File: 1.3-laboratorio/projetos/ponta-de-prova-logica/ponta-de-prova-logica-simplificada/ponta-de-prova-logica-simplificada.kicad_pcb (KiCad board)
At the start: 2 copper layers, 66 x 45.7 mm, 25 parts, among them J1 Conn_01x02, J2 TP1, SW1 SW_DPDT_x2, U1 LM339

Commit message: Ajustes finos no leiaute da PCB.
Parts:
- moved PP1 1.52 mm to (63.5, 46.7)
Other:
- board text added: "Ponta de Prova Lógica"

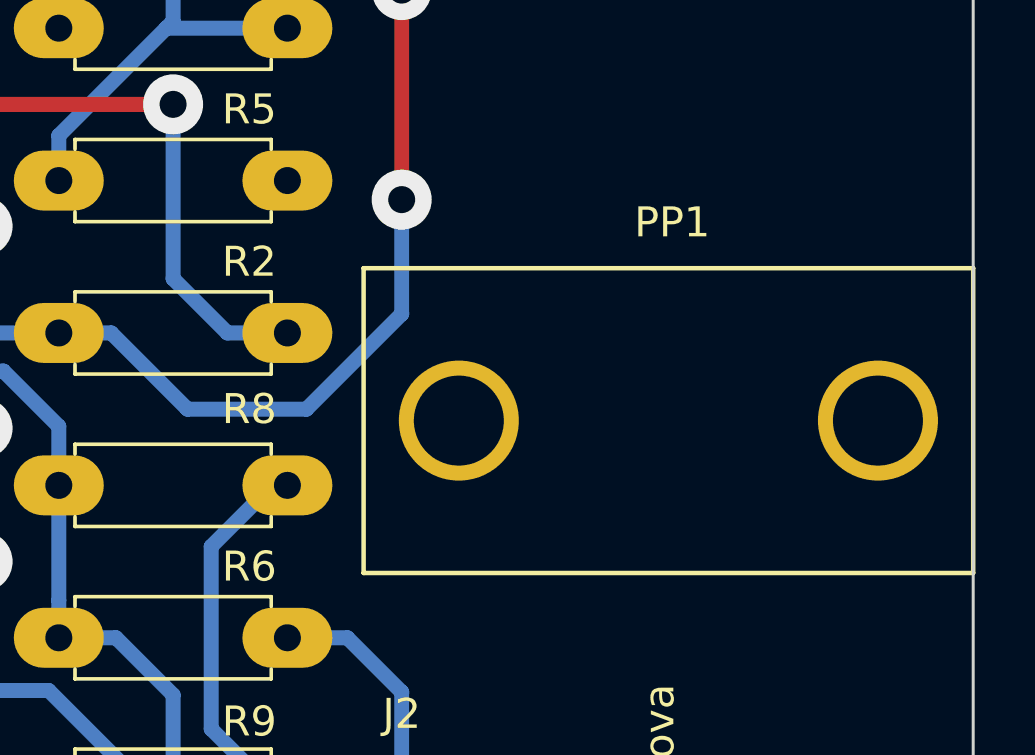
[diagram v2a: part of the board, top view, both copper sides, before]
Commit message: Ajuste no leiaute e impressão das camadas.
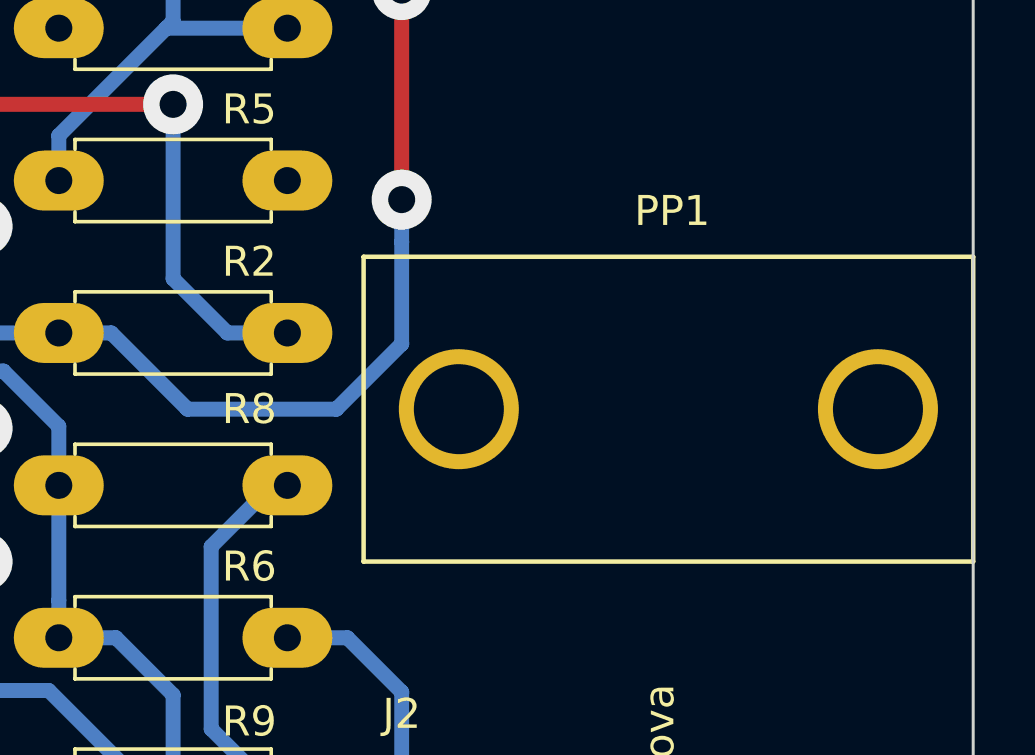
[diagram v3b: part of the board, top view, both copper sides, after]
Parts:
- moved PP1 0.38 mm to (63.5, 46.4)
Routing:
- net Net-(R1-Pad2): track 92.9 -> 93.5 mm
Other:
- board text removed: "2x 820/0.5W"
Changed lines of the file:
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@@
   (general
     (thickness 1.6)
-    (drawings 31)
-    (tracks 164)
+    (drawings 30)
+    (tracks 165)
     (zones 0)
     (modules 25)
@@
     (47 F.CrtYd user)
     (48 B.Fab user)
-    (49 F.Fab user hide)
+    (49 F.Fab user)
   )
   (setup
@@
     (visible_elements 7FFFFFFF)
     (pcbplotparams
-      (layerselection 0x00060_fffffffe)
+      (layerselection 0x00000_7fffffff)
       (usegerberextensions false)
       (usegerberattributes false)
@@
       (psa4output false)
       (plotreference true)
-      (plotvalue false)
+      (plotvalue true)
       (plotinvisibletext false)
-      (padsonsilk false)
+      (padsonsilk true)
       (subtractmaskfromsilk false)
-      (outputformat 1)
+      (outputformat 5)
       (mirror false)
       (drillshape 0)
@@
   )
   (module ponta-de-prova-fixacao-20mm-x-10mm-x-10mm (layer F.Cu)
-    (at 63.5 46.736 90)
+    (at 63.5 46.355 90)
     (fp_text reference PP1 (at 11.684 10.287 180) (layer F.SilkS)
       (effects (font (size 1 1) (thickness 0.15)))
@@
     (effects (font (size 1.25 1.25) (thickness 0.2)))
   )
-  (gr_text "2x 820/0.5W" (at 136.398 108.204 270) (layer F.Fab)
-    (effects (font (size 1 1) (thickness 0.2)))
-  )
   (gr_text ETE102 (at 77.47 23.495 90) (layer B.Cu)
     (effects (font (size 1 1) (thickness 0.2)) (justify mirror))
@@
   (segment (start 55.09 38.735) (end 53.34 38.735) (width 0.5) (layer B.Cu) (net 5))
   (segment (start 64.77 27.305) (end 64.77 34.29) (width 0.5) (layer F.Cu) (net 5))
-  (segment (start 64.77 34.29) (end 64.77 38.1) (width 0.5) (layer B.Cu) (net 5))
-  (segment (start 64.77 38.1) (end 61.595 41.275) (width 0.5) (layer B.Cu) (net 5))
-  (segment (start 61.595 41.275) (end 57.63 41.275) (width 0.5) (layer B.Cu) (net 5))
   (segment (start 57.63 41.275) (end 55.09 38.735) (width 0.5) (layer B.Cu) (net 5))
   (via (at 64.77 34.29) (size 2) (drill 0.9) (layers F.Cu B.Cu) (net 5))
   (segment (start 23.1648 32.6898) (end 24.765 32.6898) (width 0.5) (layer B.Cu) (net 5))
   (segment (start 22.86 32.385) (end 23.1648 32.6898) (width 0.5) (layer B.Cu) (net 5))
+  (segment (start 64.77 35.704213) (end 64.77 34.29) (width 0.5) (layer B.Cu) (net 5))
+  (segment (start 64.77 39.098158) (end 64.77 35.704213) (width 0.5) (layer B.Cu) (net 5))
+  (segment (start 62.593158 41.275) (end 64.77 39.098158) (width 0.5) (layer B.Cu) (net 5))
+  (segment (start 57.63 41.275) (end 62.593158 41.275) (width 0.5) (layer B.Cu) (net 5))
   (segment (start 40.005 28.575) (end 40.005 24.911999) (width 0.5) (layer B.Cu) (net 6))
   (segment (start 40.005 24.911999) (end 40.005 22.225) (width 0.5) (layer B.Cu) (net 6))
